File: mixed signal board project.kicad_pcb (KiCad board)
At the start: 4 copper layers, 70 x 70 mm, 188 parts, among them J101 USB_B_Mini, J102 Conn_01x06_Pin, J201 8P8C_Shielded, J301 Conn_01x04_Pin, J401 AudioJack3, J402 Conn_01x04_Pin, J403 Screw_Terminal_01x03, J501 USB_B_Mini, J701 Conn_01x02_Socket, J801 Conn_01x02_Socket, J901 UART_CONN, J902 CAN_CONN, SW101 SW_SPDT, SW201 SW_SPDT, SW901 SW_SPDT, U101 STM32F103C8Tx, U11 LD1117S33TR_SOT223, U12 LD1117S18TR_SOT223, U201 DP83826ERHBR, U301 ADS122C04IPW, U401 CS43L22-CNZ, U402 IMP34DT05TR, U501 CH340C, U701 DMHT6016LFJ-13, U702 DRV8701, U801 DMHT6016LFJ-13, U802 DRV8701, U901 STM32F407VGTx, Y201 25Mhz, Y901 8MHz

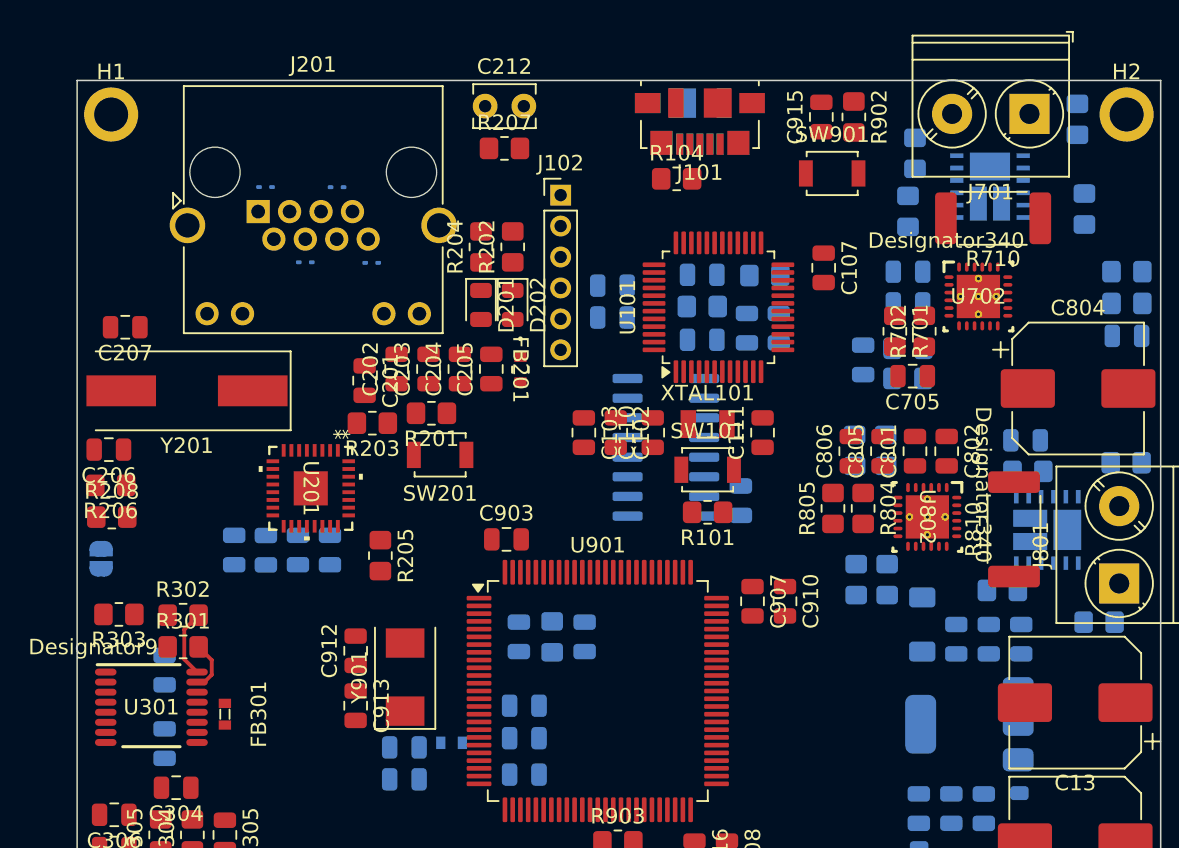
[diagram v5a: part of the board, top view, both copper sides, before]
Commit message: ethernet, usb and motor driver-2 block routed, analog and digital planes seperated
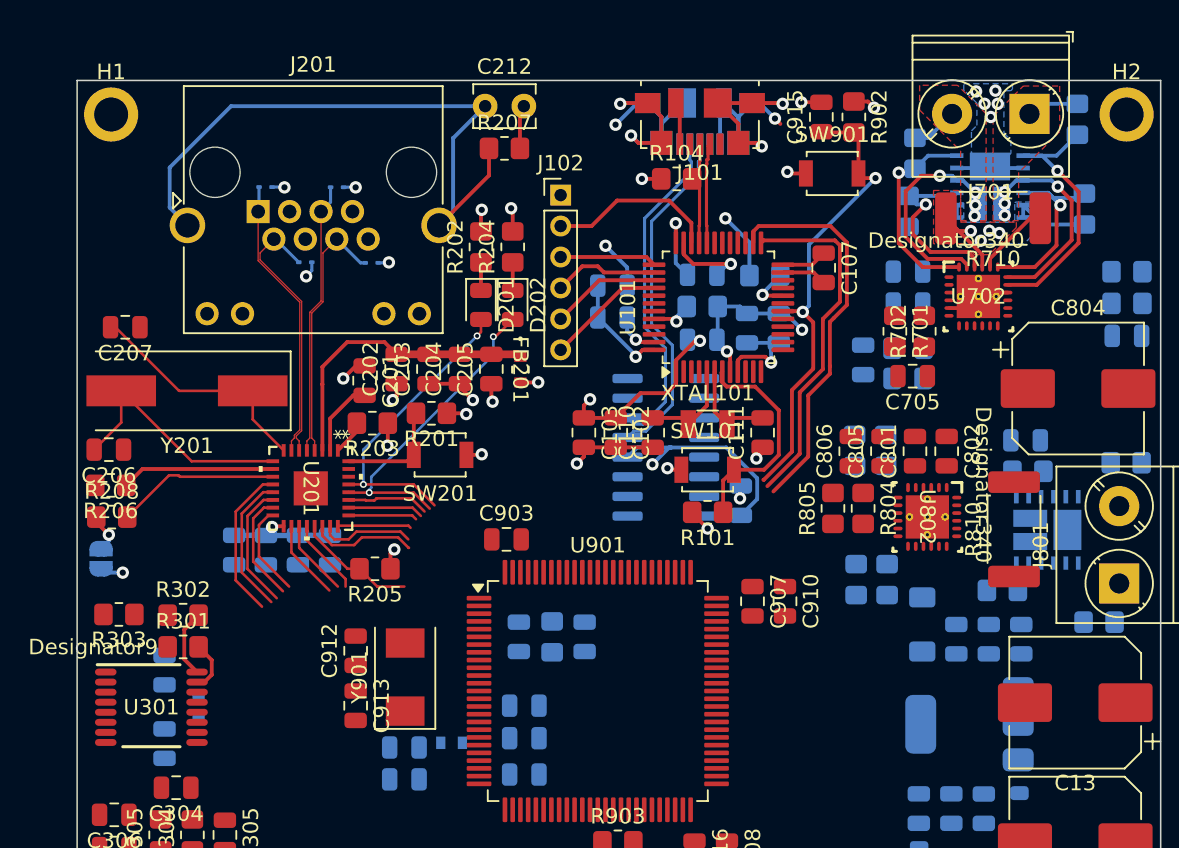
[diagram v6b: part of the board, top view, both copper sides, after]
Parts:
- FB301: moved to B.Cu
- moved R202 2.05 mm to (96.2, 64.2)
- moved R204 2.05 mm to (98.2, 64.2)
- moved FB301 1.74 mm to (77.9, 94.0)
- moved R205 0.92 mm to (89.3, 85.0), turned to 180 degrees
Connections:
- U702 pad 25: (no net) -> GND
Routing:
- net GND: track 0.00 -> 108.8 mm, vias 0 -> 29
- net +3V3: track 0.00 -> 69.2 mm, vias 0 -> 15
- net /Ethernet/RJ_45_SH: track 0.00 -> 41.5 mm
- net /STM32F407/NTRST_F407: track 0.00 -> 30.5 mm, vias 0 -> 2
- net /Debugger/JTCLK_F407: track 0.00 -> 25.4 mm
- net /Debugger/JTMS_F407: track 0.00 -> 22.8 mm
- net /USB_to_TTL/CH340_DP: track 0.00 -> 22.5 mm
- net /USB_to_TTL/CH340_DN: track 0.00 -> 21.7 mm
- net /Ethernet/ETH_COL: track 0.00 -> 20.8 mm, vias 0 -> 2
- net /Ethernet/ETH_CRS: track 0.00 -> 19.9 mm, vias 0 -> 2
- net +3.3VA: track 0.00 -> 19.3 mm
- net /Ethernet/TD_P: track 0.00 -> 18.4 mm
- net /Ethernet/RD_P: track 0.00 -> 17.6 mm
- net /Motor_Driver2/GH1_2: track 0.00 -> 17.6 mm, vias 0 -> 1
- net /Ethernet/TD_N: track 0.00 -> 17.6 mm
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- added copper zone on B.Cu, net +12V
- added copper zone on In2.Cu, net +12V
- added copper zone on In2.Cu, net +3V3
- added copper zone on F.Cu, net /Motor_Driver2/SH1_2
- added copper zone on F.Cu, net /Motor_Driver2/SH2_2
- added copper zone on B.Cu, net /Motor_Driver2/SP_2
- added copper zone on F.Cu, net /Motor_Driver2/SP_2
- added copper zone on In1.Cu, net GND

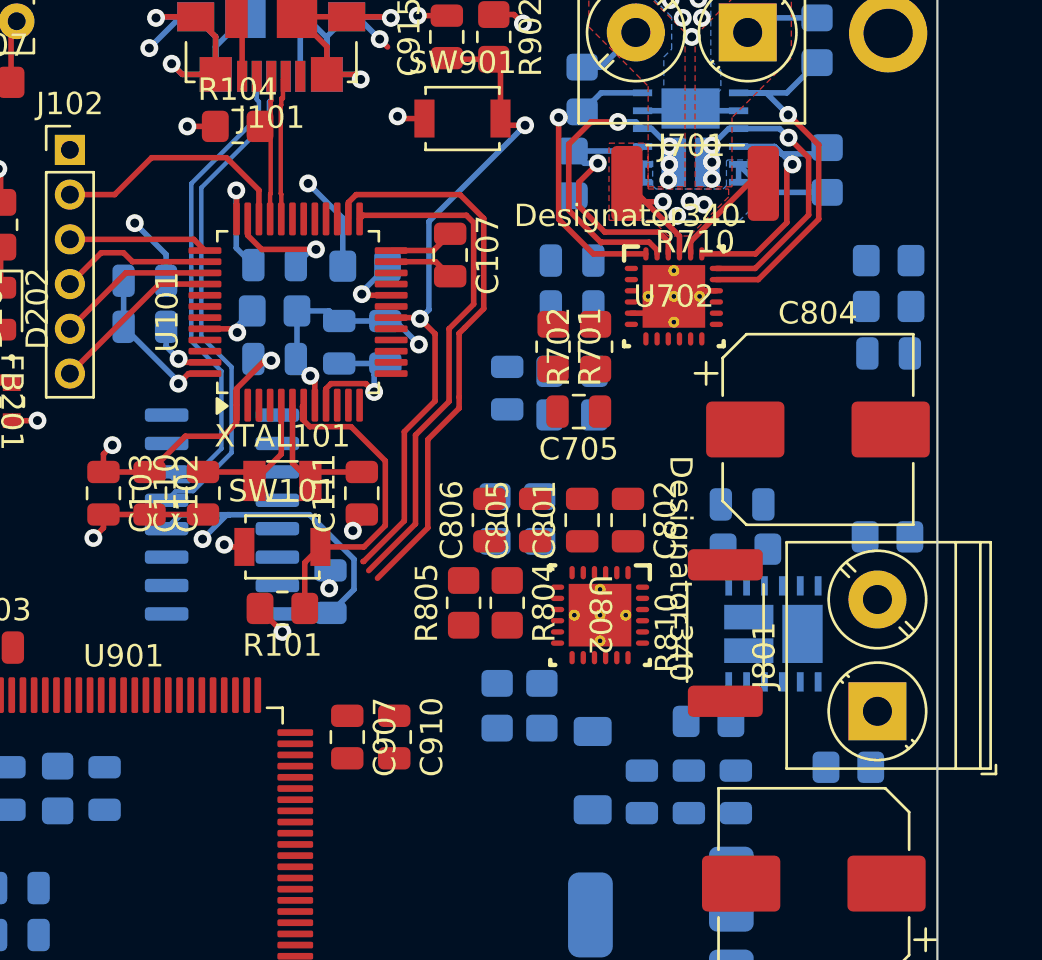
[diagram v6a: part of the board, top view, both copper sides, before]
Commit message: motor driver nsleep pin pull-up resistor connected 12V plane by 3.3V voltage divider.
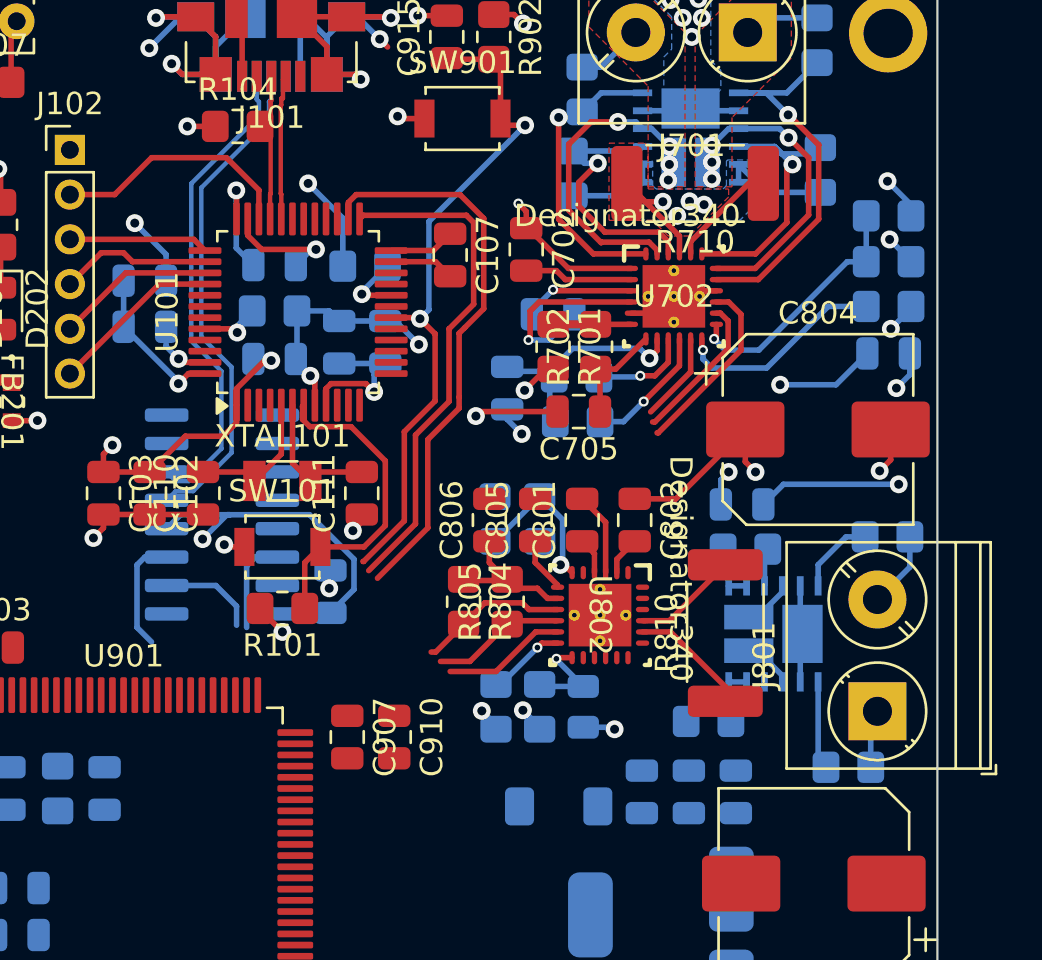
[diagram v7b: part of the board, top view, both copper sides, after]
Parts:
- added R712: 3k3, Resistor_SMD:R_0805_2012Metric_Pad1.20x1.40mm_HandSolder, B.Cu at (137.9, 65.8)
- added R812: 3k3, Resistor_SMD:R_0805_2012Metric, B.Cu at (124.2, 85.8)
- C702: moved to F.Cu
- R711, R811: value 10k -> 7k2
- moved R705 2.26 mm to (124.0, 73.0)
- moved D12 2.21 mm to (123.2, 90.2), turned to 180 degrees
- moved C702 2.11 mm to (121.7, 65.3), turned to -90 degrees
- moved R711 2.00 mm to (137.9, 63.8)
- moved R804 1.95 mm to (118.9, 81.0)
- moved R805 1.95 mm to (120.8, 81.0)
- moved R704 1.71 mm to (124.0, 71.0)
- moved C701 0.92 mm to (122.9, 68.2)
- moved R707 0.30 mm to (134.8, 61.8)
- moved C802 0.30 mm to (126.5, 77.4)
- moved R811 0.11 mm to (122.3, 85.8), turned to -90 degrees
- moved R808 0.07 mm to (120.3, 85.8)
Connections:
- R711 pad 1: +3V3 -> +12V
- R811 pad 1: +3V3 -> Net-(U802-nSLEEP)
- R811 pad 2: Net-(U802-nSLEEP) -> +12V
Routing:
- net +12V: track 4.38 -> 33.0 mm, vias 5 -> 11
- net GND: track 108.8 -> 136.5 mm, vias 29 -> 39
- net Net-(U702-nSLEEP): track 0.00 -> 11.4 mm, vias 0 -> 1
- net DVDD_2: track 0.00 -> 10.0 mm, vias 0 -> 1
- net Net-(U702-IDRIVE): track 0.00 -> 9.53 mm, vias 0 -> 1
- net Net-(U702-CPL): track 0.00 -> 8.55 mm, vias 0 -> 1
- net /Motor_Driver2/PH_2: track 0.00 -> 8.21 mm
- net Net-(U802-VREF): track 0.00 -> 7.01 mm, vias 0 -> 1
- net /Motor_Driver1/nFAULT: track 0.00 -> 6.69 mm
- net /Motor_Driver2/EN_2: track 0.00 -> 6.64 mm
- net DVDD_1: track 0.00 -> 6.61 mm
- net /Motor_Driver1/SP: track 0.00 -> 6.34 mm
- net /Motor_Driver1/SNSOUT: track 0.00 -> 5.98 mm
- net /Motor_Driver2/SNSOUT_2: track 0.00 -> 5.79 mm, vias 0 -> 1
- net /Motor_Driver1/SH2: track 0.00 -> 5.64 mm
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
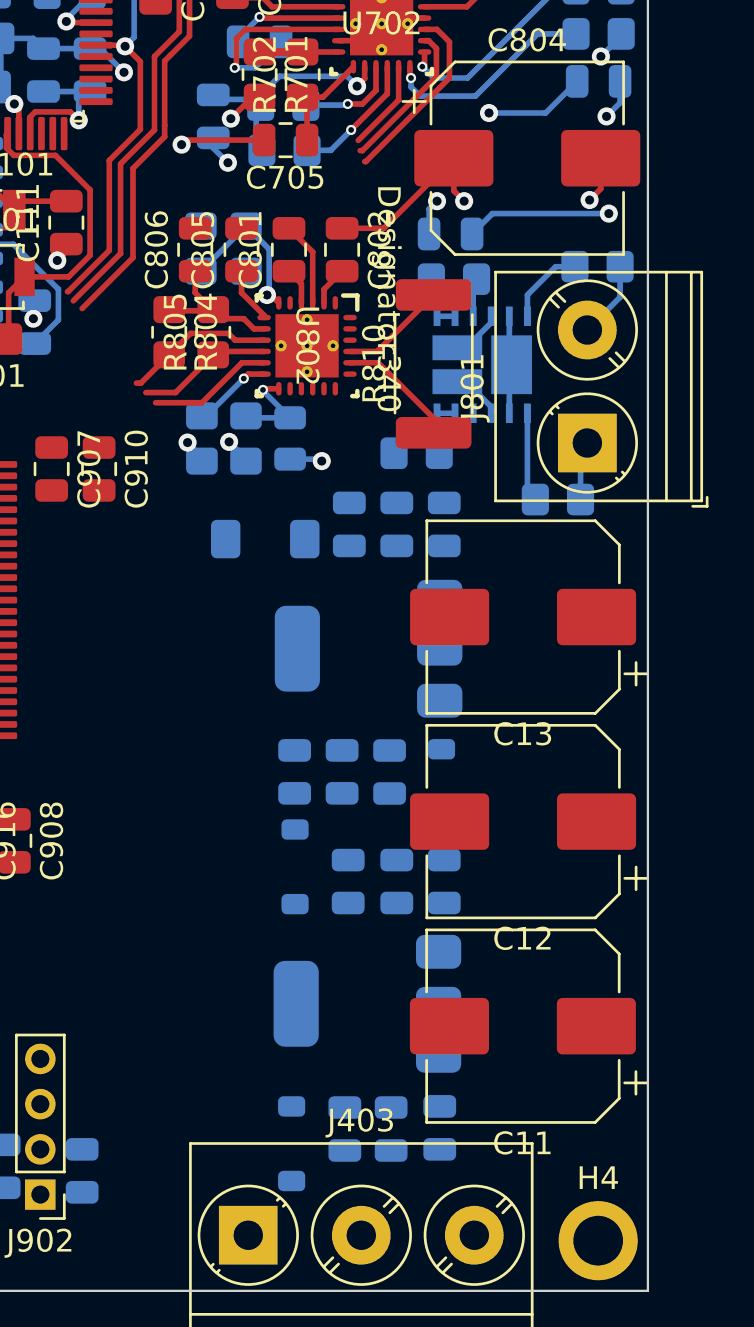
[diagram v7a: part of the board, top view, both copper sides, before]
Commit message: 1.8V voltage regülator block placed in top side to provide a solid return path
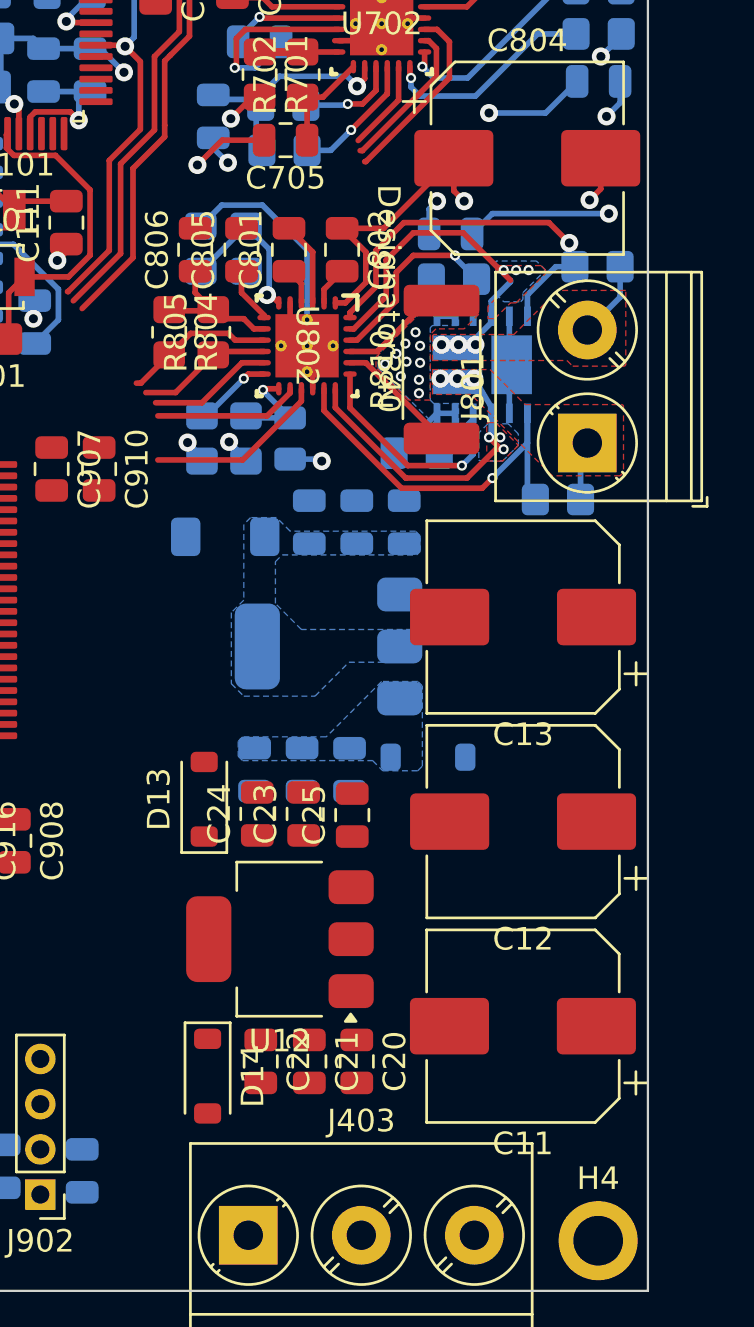
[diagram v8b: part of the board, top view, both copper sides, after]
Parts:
- C20, C21, C22, C23, C24, C25, D13, D14, U12: moved to F.Cu
- moved D13 15.7 mm to (120.5, 101.7), turned to 90 degrees
- moved C23 14.5 mm to (124.8, 102.4), turned to 90 degrees
- moved C24 14.5 mm to (122.8, 102.4), turned to 90 degrees
- moved C25 14.4 mm to (127.0, 102.4), turned to 90 degrees
- moved D14 10.0 mm to (120.6, 114.0), turned to -90 degrees
- moved C21 8.85 mm to (125.1, 113.3), turned to -90 degrees
- moved C20 8.85 mm to (127.2, 113.3), turned to -90 degrees
- moved C22 8.85 mm to (123.0, 113.3), turned to -90 degrees
- moved U12 4.81 mm to (123.8, 107.9)
- moved D12 1.77 mm to (121.4, 90.1)
- moved C16 1.77 mm to (125.1, 89.5)
- moved C19 1.77 mm to (126.9, 100.4)
- moved C15 1.77 mm to (127.2, 89.5)
- moved C17 1.77 mm to (122.7, 100.4)
- moved C18 1.77 mm to (124.8, 100.4)
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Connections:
- U802 pad 25: (no net) -> GND
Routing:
- net /Motor_Driver1/GH2: track 3.56 -> 17.6 mm, vias 0 -> 1
- net /Motor_Driver1/GH1: track 3.96 -> 17.5 mm, vias 0 -> 1
- net /Motor_Driver1/SH2: track 5.64 -> 18.6 mm, vias 0 -> 6
- net GND: track 136.5 -> 149.5 mm
- net /Motor_Driver1/SH1: track 4.87 -> 17.4 mm, vias 0 -> 6
- net /Motor_Driver1/GL1: track 0.00 -> 12.4 mm, vias 0 -> 1
- net /Motor_Driver1/GL2: track 1.70 -> 10.1 mm, vias 0 -> 1
- net /Motor_Driver1/PH: track 0.00 -> 7.98 mm
- net /Motor_Driver1/EN: track 0.00 -> 6.45 mm
- net /Motor_Driver1/SP: track 6.34 -> 11.0 mm, vias 0 -> 10
- net +12V: track 33.0 -> 37.5 mm
- added copper zone on B.Cu, net +3V3
- added copper zone on B.Cu, net /Motor_Driver1/SH1
- added copper zone on F.Cu, net /Motor_Driver1/SH1
- added copper zone on B.Cu, net /Motor_Driver1/SH2
- added copper zone on F.Cu, net /Motor_Driver1/SH2
- added copper zone on B.Cu, net /Motor_Driver1/SP
- added copper zone on F.Cu, net /Motor_Driver1/SP
- added copper zone on B.Cu, net Net-(D11-K)
